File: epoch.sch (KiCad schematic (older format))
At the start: 32 parts, among them J1 USB_OTG, J2 CONN_01X05, P3 CONN_01X10, SW1 SW_Reset, SW2 SW_Up, SW3 SW_Middle, SW4 SW_Down, U1 MIC5219-3.3BM5, U2 ATSAMD21Ennc-AU, U3 DS3231MZ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

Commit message: Final connections
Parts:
- SW1: footprint Buttons_Switches_SMD:SW_SPST_SKTDLDE010 -> Buttons_Switches_SMD:SW_SPST_B3U-3000P
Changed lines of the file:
@@
 F 0 "SW1" H 3550 6650 50  0000 L CNN
 F 1 "SW_Reset" H 3500 6490 50  0000 C CNN
-F 2 "Buttons_Switches_SMD:SW_SPST_SKTDLDE010" H 3500 6750 50  0001 C CNN
+F 2 "Buttons_Switches_SMD:SW_SPST_B3U-3000P" H 3500 6750 50  0001 C CNN
 F 3 "" H 3500 6750 50  0000 C CNN
 	1    3500 6550

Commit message: Closed
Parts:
- SW2, SW3, SW4: footprint Buttons_Switches_SMD:SW_SPST_B3U-1100P -> Buttons_Switches_SMD:SW_SPDT_EBAY_3PIN_VERT
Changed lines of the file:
@@
 F 0 "SW2" H 5300 6500 50  0000 L CNN
 F 1 "SW_Up" H 5250 6340 50  0000 C CNN
-F 2 "Buttons_Switches_SMD:SW_SPST_B3U-1100P" H 5250 6600 50  0001 C CNN
+F 2 "Buttons_Switches_SMD:SW_SPDT_EBAY_3PIN_VERT" H 5250 6600 50  0001 C CNN
 F 3 "" H 5250 6600 50  0001 C CNN
 	1    5250 6400
@@
 F 0 "SW3" H 5300 6850 50  0000 L CNN
 F 1 "SW_Middle" H 5250 6690 50  0000 C CNN
-F 2 "Buttons_Switches_SMD:SW_SPST_B3U-1100P" H 5250 6950 50  0001 C CNN
+F 2 "Buttons_Switches_SMD:SW_SPDT_EBAY_3PIN_VERT" H 5250 6950 50  0001 C CNN
 F 3 "" H 5250 6950 50  0001 C CNN
 	1    5250 6750
@@
 F 0 "SW4" H 5300 7200 50  0000 L CNN
 F 1 "SW_Down" H 5250 7040 50  0000 C CNN
-F 2 "Buttons_Switches_SMD:SW_SPST_B3U-1100P" H 5250 7300 50  0001 C CNN
+F 2 "Buttons_Switches_SMD:SW_SPDT_EBAY_3PIN_VERT" H 5250 7300 50  0001 C CNN
 F 3 "" H 5250 7300 50  0001 C CNN
 	1    5250 7100

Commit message: Correct interrupt connections to pins that actually support interrupts
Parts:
- removed C7, C8: 18pF, Capacitors_SMD:C_0805_HandSoldering, symbol C_Small
- removed Y1: 32.768kHz, Crystals:Crystal_SMD_EuroQuartz_EQ161-2pin_3.2x1.5mm, symbol Crystal
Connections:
- wire segments 116 -> 103

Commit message: New version with crystal removed and 32Khz output into XTA of 2nd RTC
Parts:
- removed Y2: 32.768kHz, Crystals:Crystal_SMD_EuroQuartz_EQ161-2pin_3.2x1.5mm, symbol Crystal
- added R6: 10K, Resistors_SMD:R_0805_HandSoldering, symbol R
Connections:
- net labels added: 32KHz
- wire segments 103 -> 101
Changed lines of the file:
@@
 L (+3.3) #PWR029
 U 1 1 5905348C
-P 6950 1100
-F 0 "#PWR029" H 6950 1150 30  0001 C CNN
-F 1 "(+3.3)" H 6950 1200 50  0000 C CNN
-F 2 "" H 6950 1100 60  0000 C CNN
-F 3 "" H 6950 1100 60  0000 C CNN
-	1    6950 1100
+P 6950 850
+F 0 "#PWR029" H 6950 900 30  0001 C CNN
+F 1 "(+3.3)" H 6950 950 50  0000 C CNN
+F 2 "" H 6950 850 60  0000 C CNN
+F 3 "" H 6950 850 60  0000 C CNN
+	1    6950 850
 	1    0    0    -1
 $EndComp
@@
 	7250 1250 6950 1250
 Wire Wire Line
-	6950 1250 6950 1100
+	6950 1250 6950 850
 Wire Wire Line
 	7250 1550 6950 1550
 Wire Wire Line
 	6950 1550 6950 1750
-$Comp
-L Crystal Y2
-U 1 1 59053F50
-P 6750 1400
-F 0 "Y2" H 6750 1550 50  0000 C CNN
-F 1 "32.768kHz" H 6750 1250 50  0000 C CNN
-F 2 "Crystals:Crystal_SMD_EuroQuartz_EQ161-2pin_3.2x1.5mm" H 6750 1400 50  0001 C CNN
-F 3 "" H 6750 1400 50  0000 C CNN
-	1    6750 1400
-	0    1    1    0
-$EndComp
-Wire Wire Line
-	7250 1350 6900 1350
-Wire Wire Line
-	6900 1350 6900 1200
-Wire Wire Line
-	6900 1200 6750 1200
-Wire Wire Line
-	6750 1200 6750 1250
-Wire Wire Line
-	7250 1450 6900 1450
-Wire Wire Line
-	6900 1450 6900 1600
-Wire Wire Line
-	6900 1600 6750 1600
-Wire Wire Line
-	6750 1600 6750 1550
 Text GLabel 8050 1250 2    60   Input ~ 0
 SDA
@@
 Wire Wire Line
 	6050 4450 6050 4550
+Text GLabel 8850 3800 2    60   Input ~ 0
+32KHz
+Wire Wire Line
+	8850 3800 8600 3800
+Wire Wire Line
+	8600 3800 8600 3750
+Wire Wire Line
+	8600 3750 8450 3750
+Text GLabel 6500 1350 0    60   Input ~ 0
+32KHz
+Wire Wire Line
+	6500 1350 7250 1350
+$Comp
+L (+3.3) #PWR034
+U 1 1 599BA2C8
+P 6650 850
+F 0 "#PWR034" H 6650 900 30  0001 C CNN
+F 1 "(+3.3)" H 6650 950 50  0000 C CNN
+F 2 "" H 6650 850 60  0000 C CNN
+F 3 "" H 6650 850 60  0000 C CNN
+	1    6650 850
+	1    0    0    -1
+$EndComp
+$Comp
+L R R6
+U 1 1 599BA606
+P 6650 1100
+F 0 "R6" V 6730 1100 50  0000 C CNN
+F 1 "10K" V 6650 1100 50  0000 C CNN
+F 2 "Resistors_SMD:R_0805_HandSoldering" V 6580 1100 50  0001 C CNN
+F 3 "" H 6650 1100 50  0000 C CNN
+	1    6650 1100
+	1    0    0    -1
+$EndComp
+Wire Wire Line
+	6650 1350 6650 1250
+Connection ~ 6650 1350
+Wire Wire Line
+	6650 950  6650 850
 $EndSCHEMATC

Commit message: Add  Automatic Switchover of Load Between a Battery
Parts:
- added C?: 10uF, Capacitors_SMD:C_0805_HandSoldering, symbol C_Small
- added Q? (x2): Q_PMOS_SGD, symbol Q_PMOS_SGD
- added R?: 470K, Resistors_SMD:R_0805_HandSoldering, symbol R
- added U?: LTC4412, Housings_TSOT-23, symbol LTC4412
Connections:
- net (GND): now also C?.1, U?.2 (GND), U?.3 (CTL)
- new net: C?.2, Q?.1 (S), Q?.1 (S), R?.1, U?.6 (SENSE)
- new net: Q?.2 (G), R?.2, U?.4 (STAT)
- new net: Q?.2 (G), U?.5 (GATE)
- new net: Q?.3 (D), U?.1 (Vin)
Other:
- note added: "Automatic Switchover of Load \nBetween a Battery and USB"
- moved on the sheet: C11, C9, D1, J2, P3, R2, R3, R4, U3

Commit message: Revert "Add  Automatic Switchover of Load Between a Battery"
This reverts commit 427980174dfe5bb42044178e8a82d6b50698685d.
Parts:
- removed C?: 10uF, Capacitors_SMD:C_0805_HandSoldering, symbol C_Small
- removed Q? (x2): Q_PMOS_SGD, symbol Q_PMOS_SGD
- removed R?: 470K, Resistors_SMD:R_0805_HandSoldering, symbol R
- removed U?: LTC4412, Housings_TSOT-23, symbol LTC4412
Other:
- note removed: "Automatic Switchover of Load \nBetween a Battery and USB"
- moved on the sheet: C11, C9, D1, J2, P3, R2, R3, R4, U3

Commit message: Update drills
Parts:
- added U6, U7, U8, U9: MH2mm, my-fp-library:MH2mm, symbol MH2mm
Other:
- note added: "Corner Mounting\nHoles"
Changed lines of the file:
@@
 LIBS:marks
 LIBS:maxim
+LIBS:marks_linear
 LIBS:epoch-cache
 EELAYER 25 0
@@
 Wire Wire Line
 	6650 950  6650 850
+$Comp
+L MH2mm U6
+U 1 1 59C46AF5
+P 10350 2400
+F 0 "U6" H 10450 2400 60  0001 C CNN
+F 1 "MH2mm" H 10350 2700 60  0001 C CNN
+F 2 "my-fp-library:MH2mm" H 10350 2400 60  0001 C CNN
+F 3 "" H 10350 2400 60  0001 C CNN
+	1    10350 2400
+	1    0    0    -1
+$EndComp
+$Comp
+L MH2mm U7
+U 1 1 59C46D36
+P 10350 2550
+F 0 "U7" H 10450 2550 60  0001 C CNN
+F 1 "MH2mm" H 10350 2850 60  0001 C CNN
+F 2 "my-fp-library:MH2mm" H 10350 2550 60  0001 C CNN
+F 3 "" H 10350 2550 60  0001 C CNN
+	1    10350 2550
+	1    0    0    -1
+$EndComp
+$Comp
+L MH2mm U8
+U 1 1 59C46DAD
+P 10350 2700
+F 0 "U8" H 10450 2700 60  0001 C CNN
+F 1 "MH2mm" H 10350 3000 60  0001 C CNN
+F 2 "my-fp-library:MH2mm" H 10350 2700 60  0001 C CNN
+F 3 "" H 10350 2700 60  0001 C CNN
+	1    10350 2700
+	1    0    0    -1
+$EndComp
+$Comp
+L MH2mm U9
+U 1 1 59C46E3F
+P 10350 2850
+F 0 "U9" H 10450 2850 60  0001 C CNN
+F 1 "MH2mm" H 10350 3150 60  0001 C CNN
+F 2 "my-fp-library:MH2mm" H 10350 2850 60  0001 C CNN
+F 3 "" H 10350 2850 60  0001 C CNN
+	1    10350 2850
+	1    0    0    -1
+$EndComp
+Text Notes 10000 2350 0    60   ~ 0
+Corner Mounting\nHoles
 $EndSCHEMATC

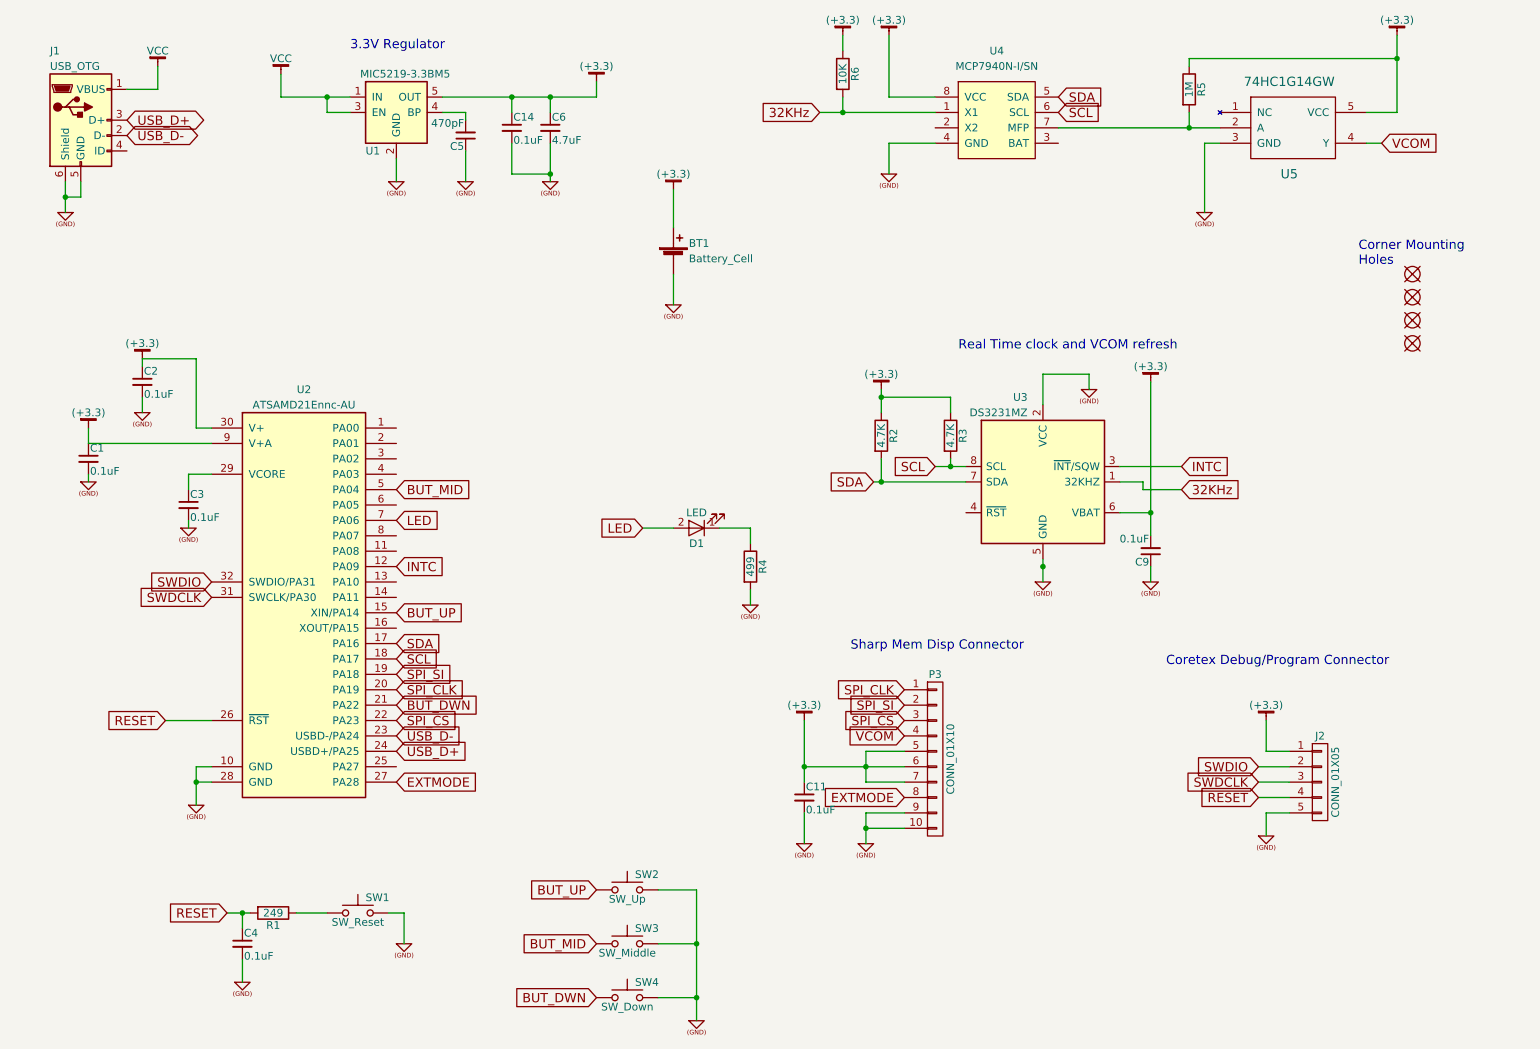
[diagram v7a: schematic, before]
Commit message: Use same connector for hotswap
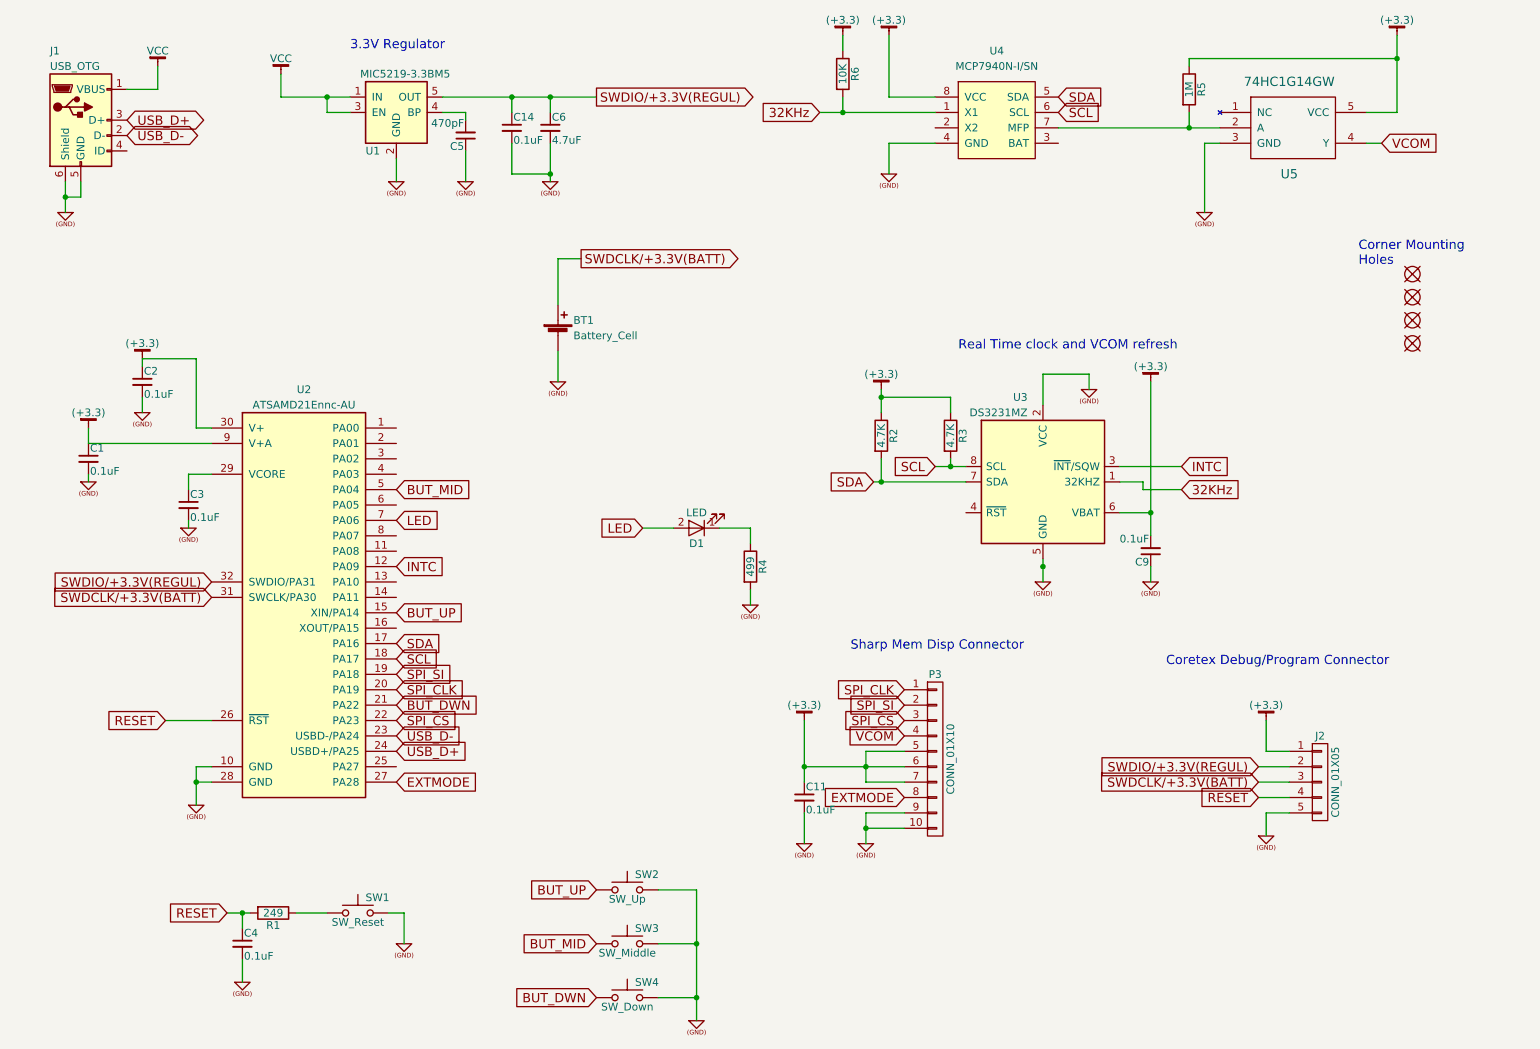
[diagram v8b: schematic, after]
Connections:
- net (+3.3): no longer BT1.1 (+), C14.1, C6.1, U1.5 (OUT)
- net SWDCLK renamed SWDCLK/+3.3V(BATT)
- net SWDCLK/+3.3V(BATT): now also BT1.1 (+)
- net SWDIO renamed SWDIO/+3.3V(REGUL)
- net SWDIO/+3.3V(REGUL): now also C14.1, C6.1, U1.5 (OUT)
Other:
- moved on the sheet: BT1
